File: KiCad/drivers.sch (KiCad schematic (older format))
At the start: 14 parts, among them J10 Screw_Terminal_01x04, J11 Screw_Terminal_01x02, J7 Screw_Terminal_01x04, J8 Screw_Terminal_01x04, J9 Screw_Terminal_01x04, U2 MCP23017_SS

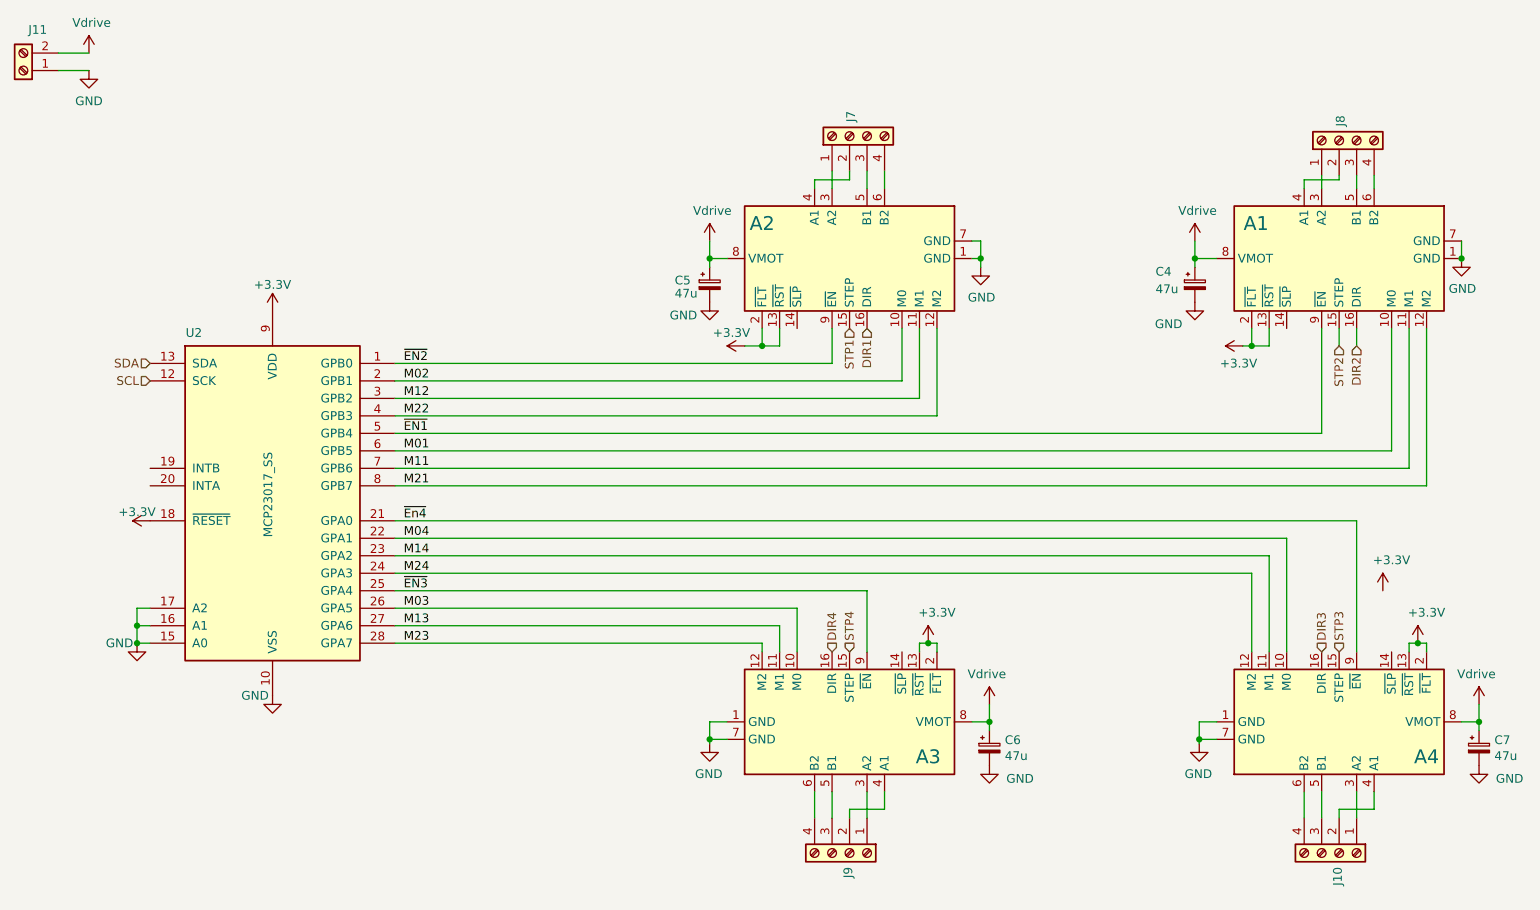
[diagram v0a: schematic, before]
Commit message: Fixed missing BOOT signal and some ERC errors
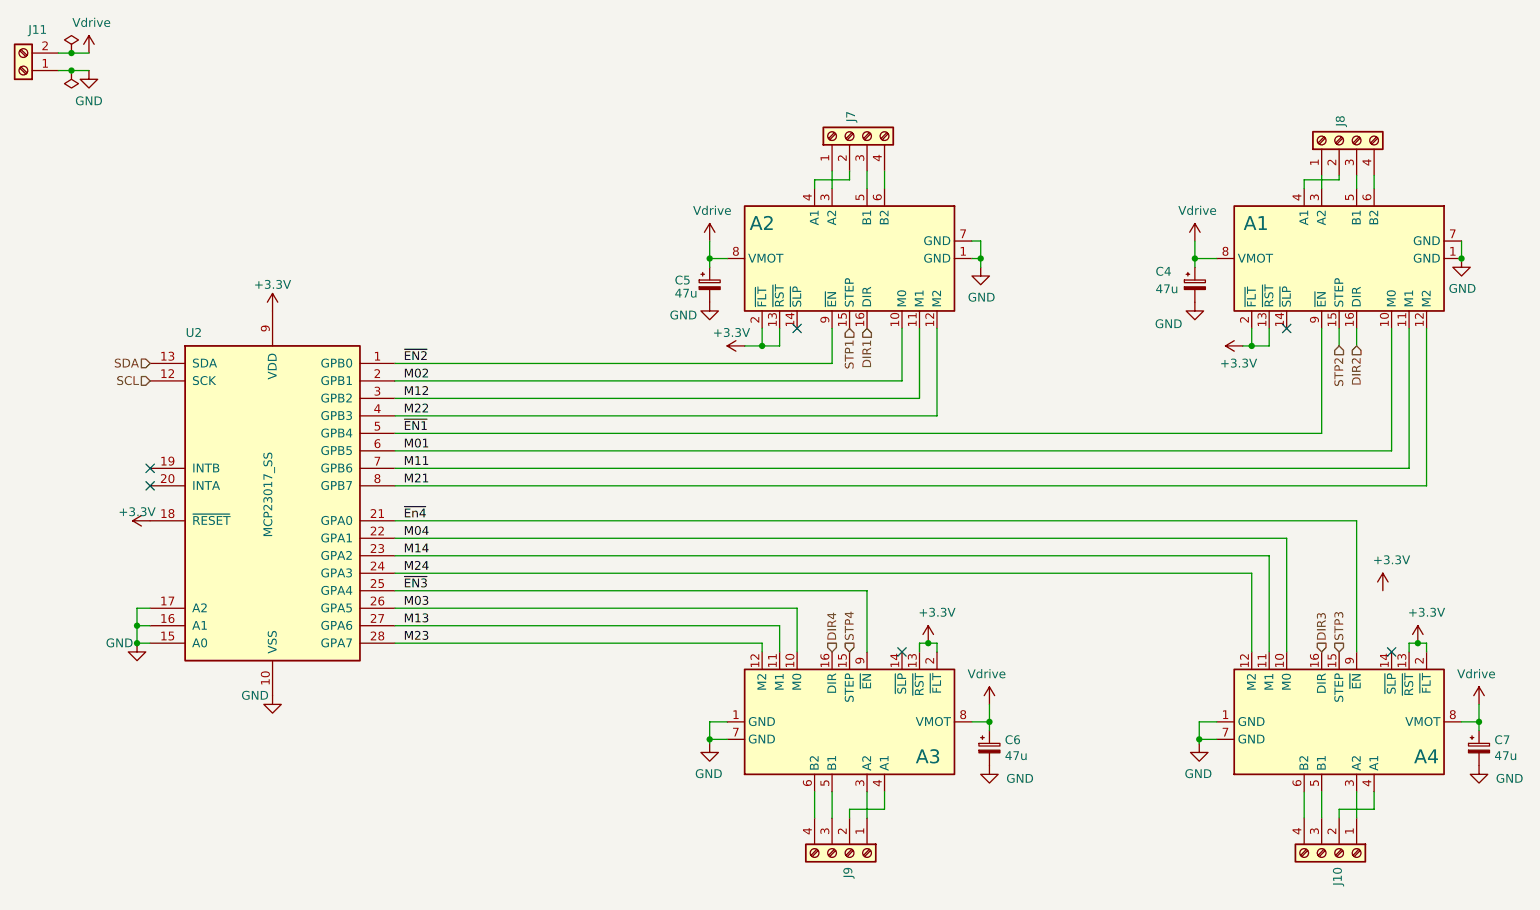
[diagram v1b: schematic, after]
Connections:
- no-connect marks 0 -> 6
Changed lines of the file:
@@
 $EndComp
 Wire Wire Line
-	1700 1225 1525 1225
-Wire Wire Line
-	1525 1325 1700 1325
+	1700 1225 1600 1225
+Wire Wire Line
+	1525 1325 1600 1325
 Text HLabel 8850 4650 1    50   Input ~ 0
 STP3
@@
 Wire Wire Line
 	8025 2400 8025 2450
+NoConn ~ 9150 4650
+NoConn ~ 8550 2800
+NoConn ~ 5750 2800
+NoConn ~ 6350 4650
+NoConn ~ 2050 3600
+NoConn ~ 2050 3700
+$Comp
+L power:PWR_FLAG #FLG0102
+U 1 1 5FF17B81
+P 1600 1225
+F 0 "#FLG0102" H 1600 1300 50  0001 C CNN
+F 1 "PWR_FLAG" H 1525 1525 50  0001 C CNN
+F 2 "" H 1600 1225 50  0001 C CNN
+F 3 "~" H 1600 1225 50  0001 C CNN
+	1    1600 1225
+	1    0    0    -1
+$EndComp
+Connection ~ 1600 1225
+Wire Wire Line
+	1600 1225 1525 1225
+$Comp
+L power:PWR_FLAG #FLG0103
+U 1 1 5FF1828E
+P 1600 1325
+F 0 "#FLG0103" H 1600 1400 50  0001 C CNN
+F 1 "PWR_FLAG" H 1525 1625 50  0001 C CNN
+F 2 "" H 1600 1325 50  0001 C CNN
+F 3 "~" H 1600 1325 50  0001 C CNN
+	1    1600 1325
+	-1   0    0    1
+$EndComp
+Connection ~ 1600 1325
+Wire Wire Line
+	1600 1325 1700 1325
 $EndSCHEMATC
